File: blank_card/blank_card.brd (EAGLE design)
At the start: 100 x 80 mm, 1 part, among them J1 09231486921

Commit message: changed pinouts for the boards, next I have to make accomodations for new pinouts and the USB selector system
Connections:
- new net 24V/12V: J1.20, J1.21, J1.22, J1.36, J1.37, J1.5, J1.6
- new net 3.3V: J1.23, J1.7
- new net 5V: J1.38, J1.39
- new net CS_1: J1.8
- new net CS_10: J1.26
- new net CS_11: J1.27
- new net CS_12: J1.28
- new net CS_13: J1.29
- new net CS_14: J1.30
- new net CS_15: J1.45
- new net CS_2: J1.9
- new net CS_3: J1.10
- new net CS_4: J1.11
- new net CS_5: J1.12
- new net CS_6: J1.13
- new net CS_7: J1.14
- new net CS_8: J1.24
- new net CS_9: J1.25
- new net GND: J1.1, J1.17, J1.18, J1.19, J1.2, J1.3, J1.33, J1.34, J1.35, J1.4
- new net MISO: J1.41
- new net MOSI: J1.42
- new net RESET: J1.48
- new net SCK: J1.40
- new net SCL: J1.44
- new net SDA: J1.43
- new net USB1_D+: J1.16
- new net USB1_D-: J1.15
- new net USB2_D+: J1.32
- new net USB2_D-: J1.31
- new net USB3_D+: J1.47
- new net USB3_D-: J1.46

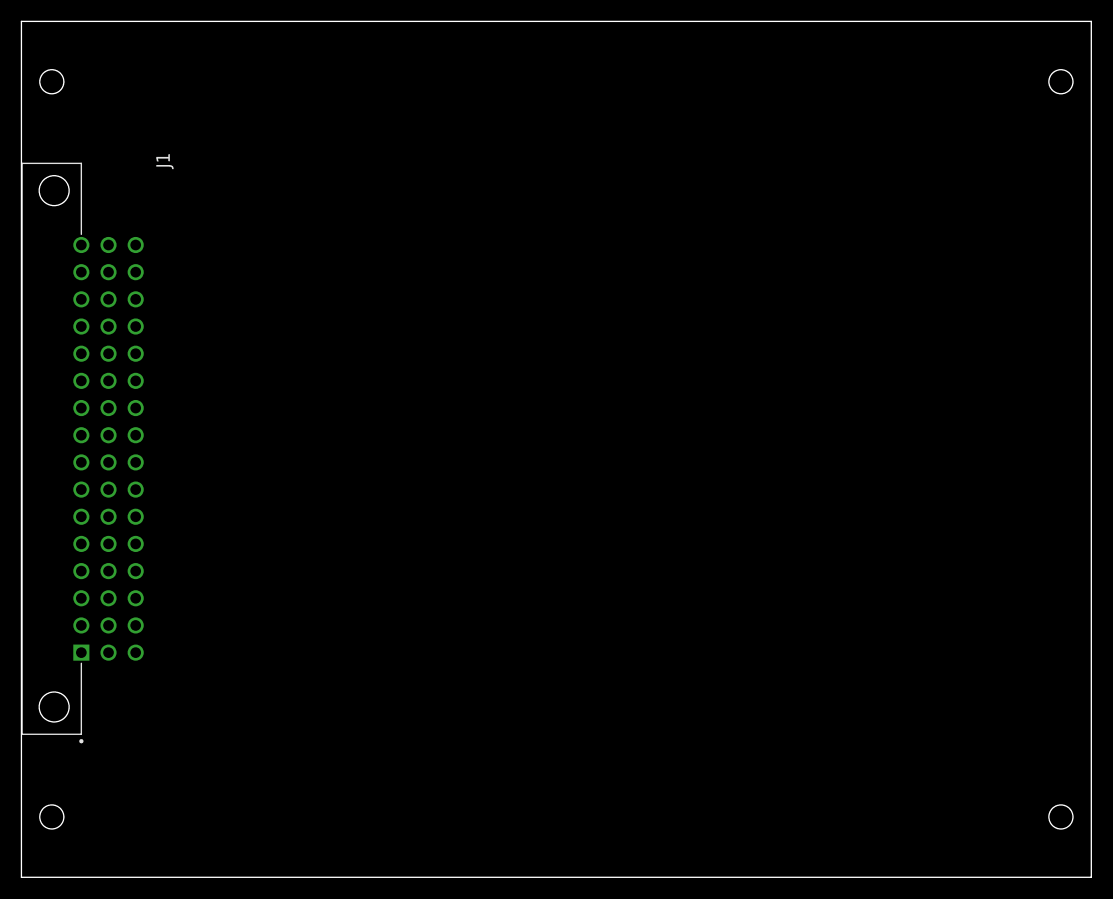
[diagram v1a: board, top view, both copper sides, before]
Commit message: made card holes bigger, started usb port work, but I'm not done that part yet
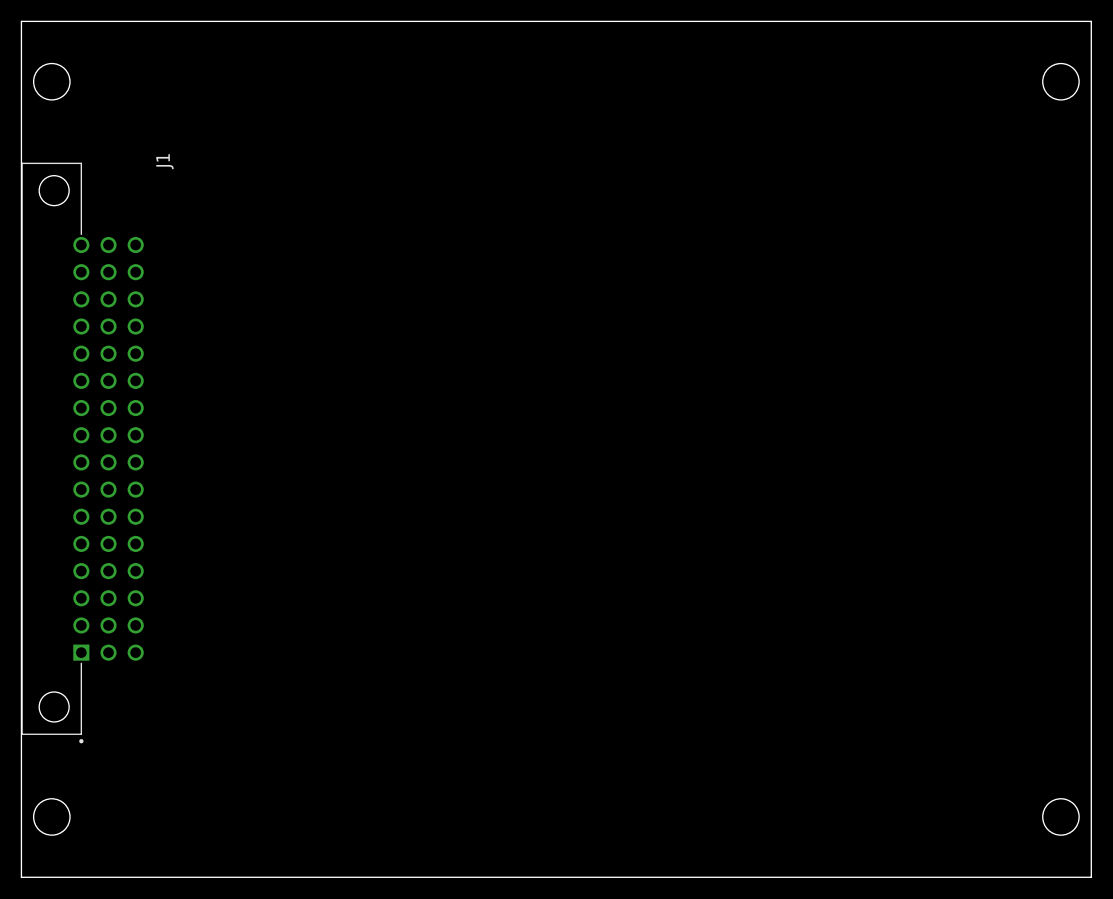
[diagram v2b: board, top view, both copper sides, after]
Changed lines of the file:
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@@
 <wire x1="100" y1="80" x2="0" y2="80" width="0" layer="20"/>
 <wire x1="0" y1="80" x2="0" y2="0" width="0" layer="20"/>
-<hole x="2.84" y="5.64" drill="2.25"/>
-<hole x="2.84" y="74.36" drill="2.25"/>
-<hole x="97.16" y="74.36" drill="2.25"/>
-<hole x="97.16" y="5.64" drill="2.25"/>
+<hole x="2.84" y="5.64" drill="3.4"/>
+<hole x="2.84" y="74.36" drill="3.4"/>
+<hole x="97.16" y="74.36" drill="3.4"/>
+<hole x="97.16" y="5.64" drill="3.4"/>
 </plain>
 <attributes>
